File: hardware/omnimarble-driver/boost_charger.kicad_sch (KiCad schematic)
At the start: 42 parts, among them K1 HF3FF-12V, K2 HF3FF-12V, Q1 MMBT3904, Q2 MMBT3904, Q3 MMBT3904, Q91 AOD66923, U4 UC3843B, U5 CJ431

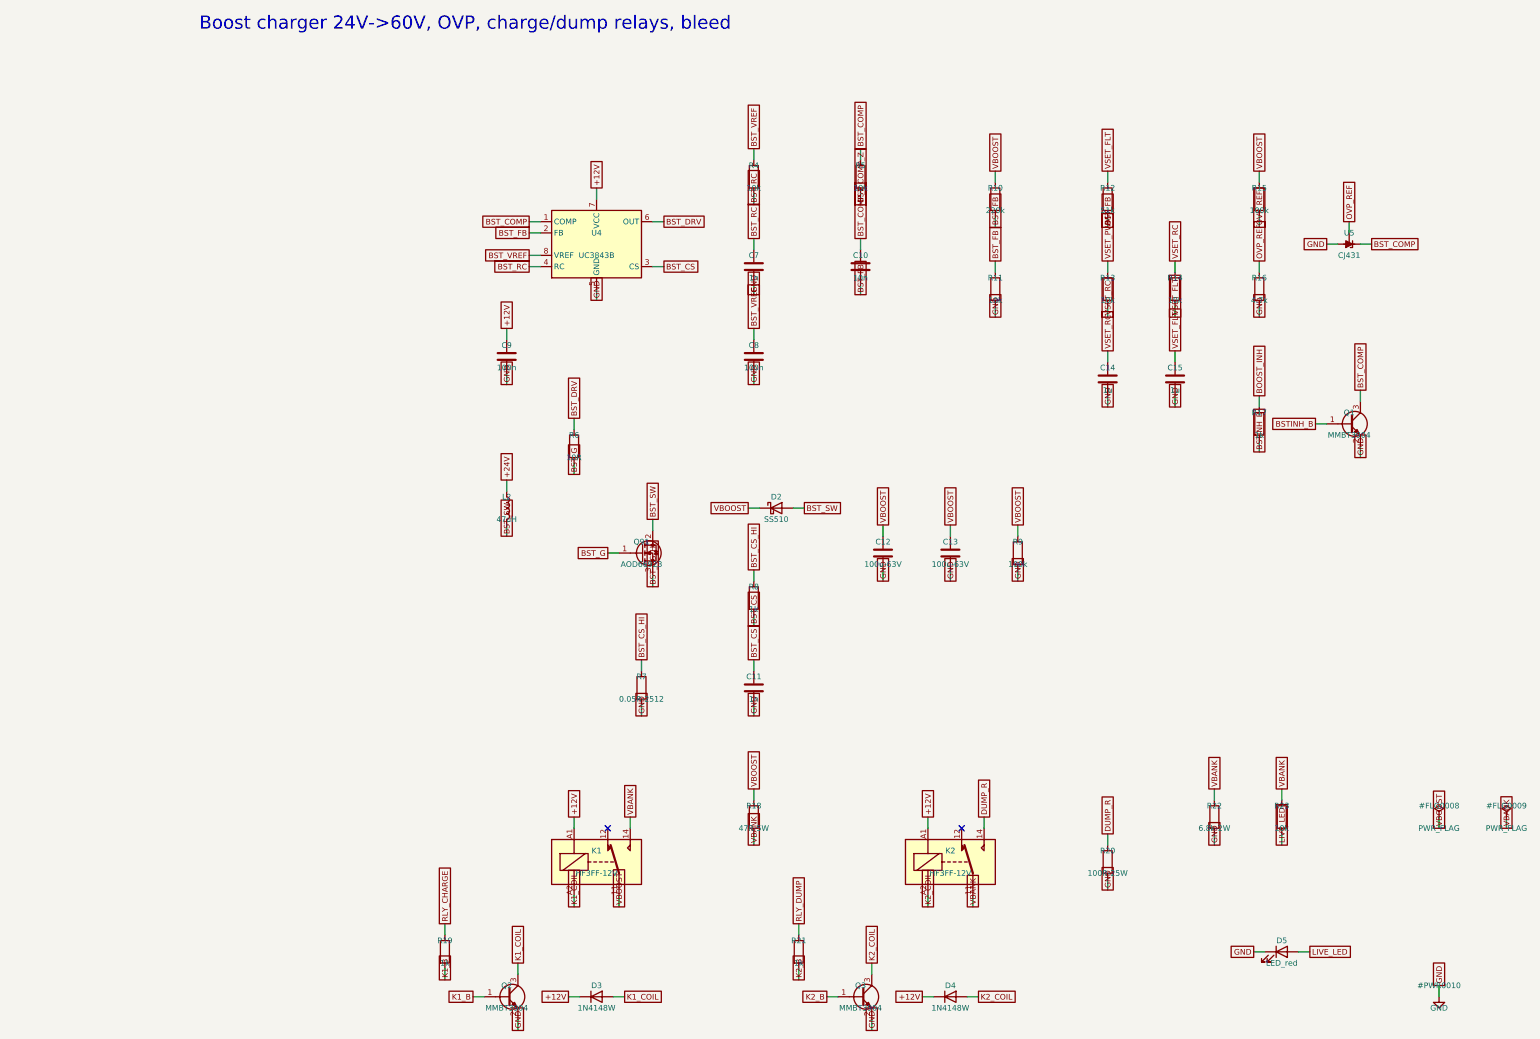
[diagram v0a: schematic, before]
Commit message: Address external design review: boost FB + OVP redesign, BOM freeze
Review findings accepted and fixed (each verified by machine check):

1. Boost feedback network was wrong (confirmed: as-drawn spanned
   54-68V with PWM inverted vs the comment). Redesigned: RT/RB/RJ =
   100k/10k/9.1k with the exact transfer function documented in the
   schematic and design-calcs.md. PWM=0 (MCU-dead state) commands
   55.0V; full PWM commands 18.7V (below the 24.5V converter floor).
   New calcs.py asserts both endpoints.
2. OVP tripped at 55.6V, not the claimed 63V (confirmed). Redesigned:
   CJ431 (+/-0.5%) + 100k/4.3k 1% -> 60.5V nominal, 59.1-62.0V across
   tolerances. Protection ladder asserted in calcs.py: 55V operating
   < 59.1V trip-min, 62.0V trip-max < 63V cap rating - 1V. Operating
   ceiling deliberately reduced 60->55V to keep the bands disjoint.
3. BOM/schematic controller split-brain: bom.csv was stale
   (pre-UC3843 swap); regenerated from parts.py. Both now UC3843B.
4. High-power placeholders now real orderable parts (LCSC-verified):
   47R/5W SQM cement C5807995, dump redesigned to 2x 100R/10W cement
   in series C216413 (no 20-25W part stocked on LCSC; 5.3s to <5V),
   50mR/3W 2512 C2994645, 63V/35V electrolytics C28241/C176666, 10uH
   Sunlord C79272, MINI fuses+Keystone 3568 holders, buzzer, Pico
   sockets/breakout headers. Single documented exception: the 6.8k/2W
   bleed (CRH2512J6K80E04Z) is marked ORDER-REVIEW because LCSC's
   search is uncrawlable - validate.py allowlists it visibly.
5. validate.py pulled forward from the fab phase: fails on unknown
   footprints, blank LCSC on machine-placed parts, missing Variant
   fields, and duplicate refs; generates per-variant gate-rail BOMs
   (bom_rail_emit/recv.csv). Caught two bad footprint names.
6. Paralleling constraints now on the schematic (same-lot FETs,
   symmetric copper, <25mm gate loops, driver return at shunt star).
7. Fail-safe defaults hardened: MCU_FIRE and FIRE_GATED get explicit
   pulldow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
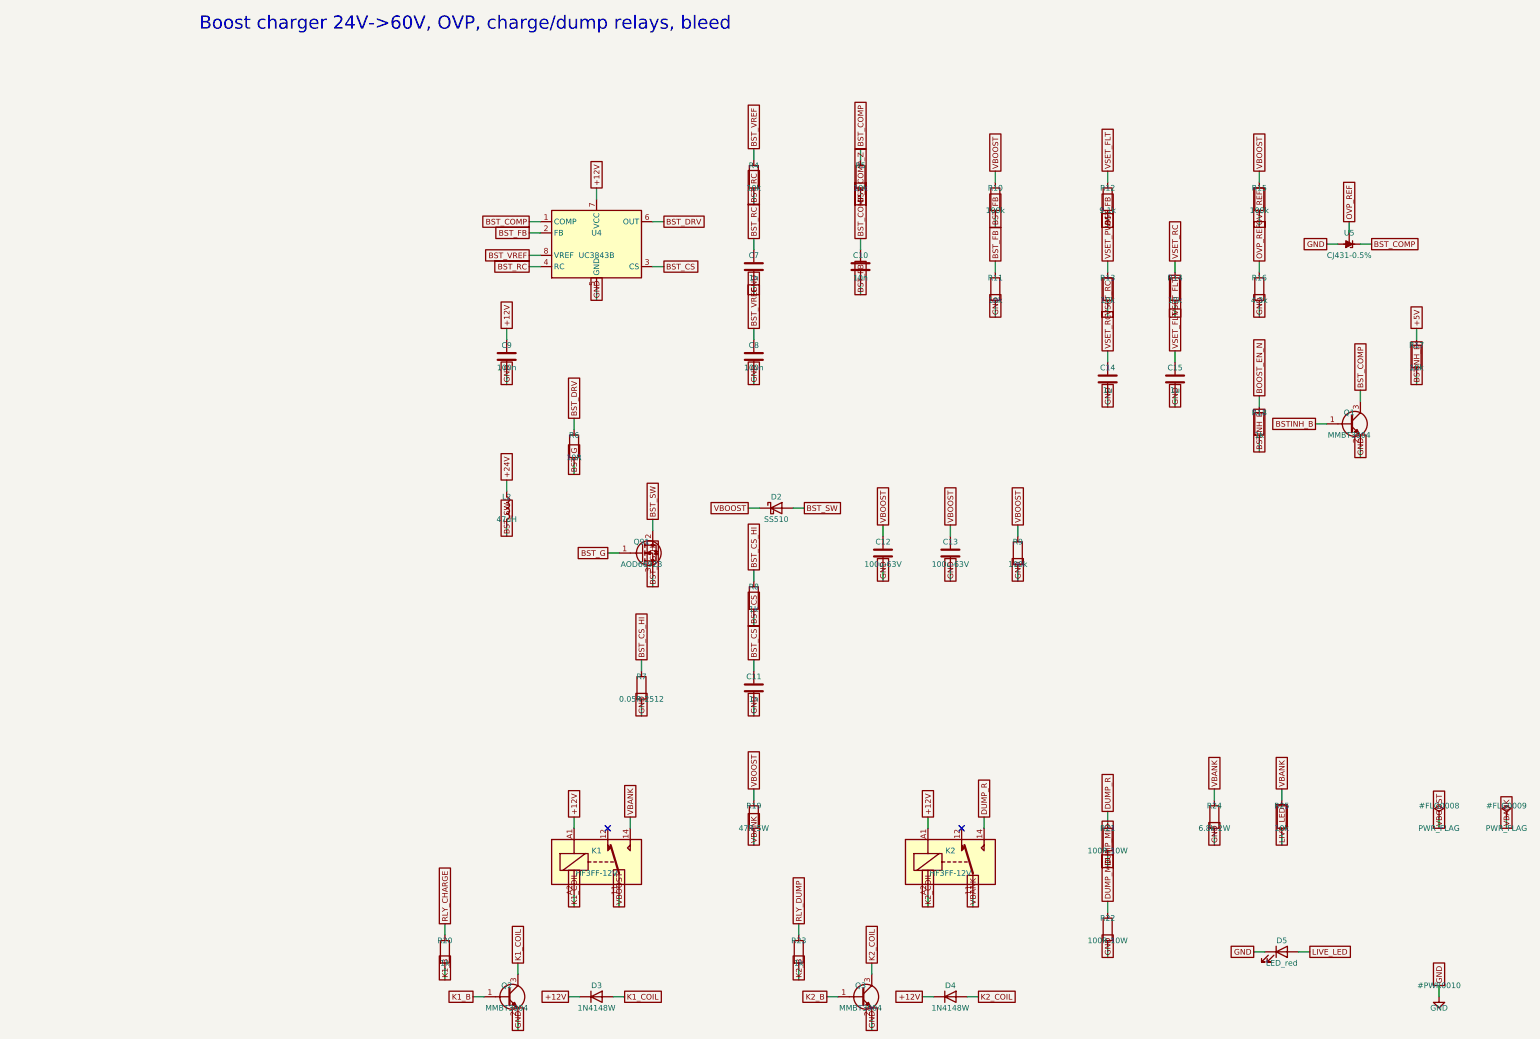
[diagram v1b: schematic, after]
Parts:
- added R24: 6.8k-2W, Resistor_SMD:R_2512_6332Metric, symbol Device:R
- added R25: 10k, Resistor_SMD:R_0603_1608Metric, symbol Device:R
- C10: LCSC (none) -> C57112
- C12, C13: LCSC (none) -> C28241
- R10: value 220k -> 100k; LCSC C22961 -> C25803
- R12: value 51k -> 9.1k; LCSC C23196 -> C23260
- R16: value 4.7k -> 4.3k; LCSC C23162 -> C23159
- R17: value 1k -> 10k; LCSC C21190 -> C25804
- R18: value 47R-5W -> 1k; footprint Resistor_SMD:R_2512_6332Metric -> Resistor_SMD:R_0603_1608Metric; LCSC (none) -> C21190
- R19: value 1k -> 47R-5W; footprint Resistor_SMD:R_0603_1608Metric -> Resistor_THT:R_Box_L26.0mm_W5.0mm_P20.00mm; LCSC C21190 -> C5807995
- R20: value 100R-25W -> 1k; footprint Resistor_SMD:R_2512_6332Metric -> Resistor_SMD:R_0603_1608Metric; LCSC (none) -> C21190
- R21: value 1k -> 100R-10W; footprint Resistor_SMD:R_0603_1608Metric -> Resistor_THT:R_Radial_Power_L11.0mm_W7.0mm_P5.00mm; LCSC C21190 -> C216413
- R22: value 6.8k-2W -> 100R-10W; footprint Resistor_SMD:R_2512_6332Metric -> Resistor_THT:R_Radial_Power_L11.0mm_W7.0mm_P5.00mm; LCSC (none) -> C216413
- R23: value 10k -> 1k; LCSC C25804 -> C21190
- R7: LCSC (none) -> C2994645
- U5: value CJ431 -> CJ431-0.5%
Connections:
- net BSTINH_B: now also R18.2
- net DUMP_R: now also R21.1; no longer R20.1
- net GND: now also R24.2; no longer R20.2
- net K1_B: now also R20.2; no longer R19.2
- net K2_B: now also R23.2; no longer R21.2
- net LIVE_LED: now also R25.2; no longer R23.2
- net RLY_CHARGE: now also R20.1; no longer R19.1
- net RLY_DUMP: now also R23.1; no longer R21.1
- net VBANK: now also R19.2, R24.1, R25.1; no longer R18.2, R22.1, R23.1
- net VBOOST: now also R19.1; no longer R18.1
- net BOOST_INH renamed +5V
- new net BOOST_EN_N: R18.1
- new net DUMP_MID: R21.2, R22.1

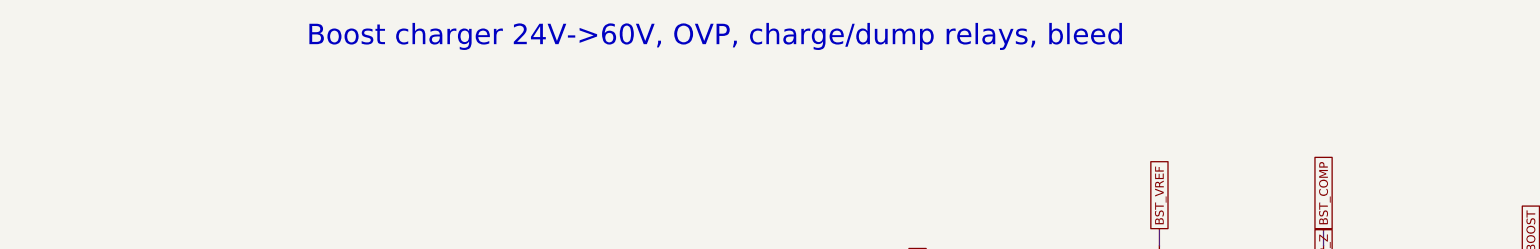
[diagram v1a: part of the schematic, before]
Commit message: Re-audit hygiene fixes: stale labels, COMMON variant, production gate
All six re-audit findings addressed:
1. Rail variant BOMs now include Variant=COMMON parts (J1 RAIL-IDC
   appears in both bom_rail_emit.csv and bom_rail_recv.csv).
2. design-calcs.md headings derive from V_BANK_MAX instead of
   hardcoded "60V" strings.
3. OVP reference wording unified to CJ431 +/-0.5% everywhere (the
   math already used ref_tol=0.005; text now matches).
4. Stale "57.2V OVP floor" magic number in the boost comment replaced
   with a reference to the calcs.py protection-ladder asserts.
5. validate.py --production mode: ORDER-REVIEW placeholder LCSC
   values fail (exit 1) at fab/assembly export; review mode warns.
   Verified: production exit code 1 on the 6.8k bleed placeholder.
6. Boost capability wording is now "24.5-55V operating (63V-rated
   bank)" in the schematic, sheet comments, and parts.py.

Re-verified: calcs 18/18 PASS, ERC 0 both projects, netlist
assertions pass, validate review-mode PASS with visible WARN,
rail BOMs 13/7 parts. PDFs refreshed.

Co-Authored-By: Claude Fable 5 <noreply@anthropic.com>
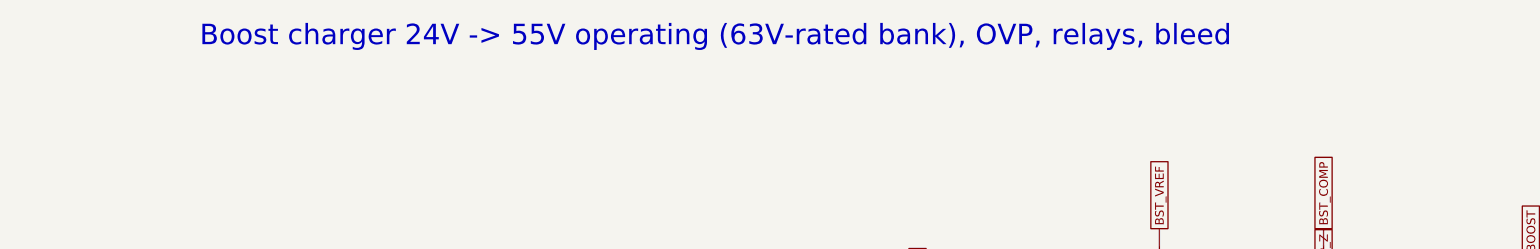
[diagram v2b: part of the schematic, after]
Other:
- note added: "Boost charger 24V -> 55V operating (63V-rated bank), OVP, relays, bleed"
- note removed: "Boost charger 24V->60V, OVP, charge/dump relays, bleed"

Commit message: Datasheet-exact footprints, placement engine, scripted PCB router WIP
- gen_footprints.py: TOLL-8, D2PAK (cathode-tab corrected), 5930 shunt,
  9.5mm barrier, HF3FF relay land patterns; drop _DRAFT footprints
- placement.py: 220x150 board plan, pulse zone polygons derived from
  package pad windows, shelf-packed clusters, Kelvin/manual tracks
- gen_pcb.py: netlist->board generator with zone builder, via stitching,
  pad-in-zone assertions, straggler/GND-drop/escape pre-routes and a
  negotiated-congestion (PathFinder-lite) signal router + greedy cleanup
- debug_route.py/debug_map.py/debug_j7.py: router diagnostics

Co-Authored-By: Claude Fable 5 <noreply@anthropic.com>
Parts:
- K1, K2: footprint omnimarble:Relay_HF3FF_T73_DRAFT -> omnimarble:Relay_HF3FF_T73

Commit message: Driver PCB: resolve review blockers (2oz trace width, R24 BOM, validators)
External review caught real fab-readiness issues; all resolved:
- BLOCKER 2oz trace width: ISNS Kelvin pair was 0.1mm (a 1oz spec; JLC 2oz min
  trace/space is 0.15mm). Widened to 0.15mm -> ~0.17mm pair spacing (both >=
  0.15mm 2oz min). Scoped `isns_kelvin_pair` rule in .kicad_dru blesses the
  sub-0.2mm pair spacing (A.NetName match); clearance to all other nets stays
  0.2mm. min_track_width -> 0.15.
- MAJOR width source-of-truth: NET_WIDTHS["ISNS_P/N"]=0.15 is now the single
  value; local_finish narrows to it, validate_widths checks it -> PASS.
- BLOCKER R24 6.8k-2W BOM placeholder: no verified JLC C-number and 2W is
  marginal in 2512 -> marked LCSC=HAND-INSTALL (explicit, exclude from CPL,
  user-sourced). validate.py --production PASSes with a NOTE.
- MAJOR check_netlist GATE1-6: stale J11 assertion (breakout removed) ->
  asserts comparator + Pico-socket topology. All netlist assertions PASS.
- CONCERN gate-drive route inequality: documented as an explicit WAIVER in
  BOARD_OVERVIEW.md (per-FET gate resistors + us-scale pulse app mitigate).
- Fixed the wrong 0.089mm/1oz capability claim in BOARD_OVERVIEW + memory.

Final: 0 electrical DRC / 0 unconnected / 0 parity; validate + validate_widths
+ check_netlist + calcs all PASS; 14 cosmetic silk warnings.

Co-Authored-By: Claude Fable 5 <noreply@anthropic.com>
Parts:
- R24: LCSC ORDER-REVIEW -> HAND-INSTALL
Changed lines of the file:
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@@
 			)
 		)
-		(property "LCSC" "ORDER-REVIEW"
+		(property "LCSC" "HAND-INSTALL"
 			(at 199.39 199.39 0)
 			(show_name no)

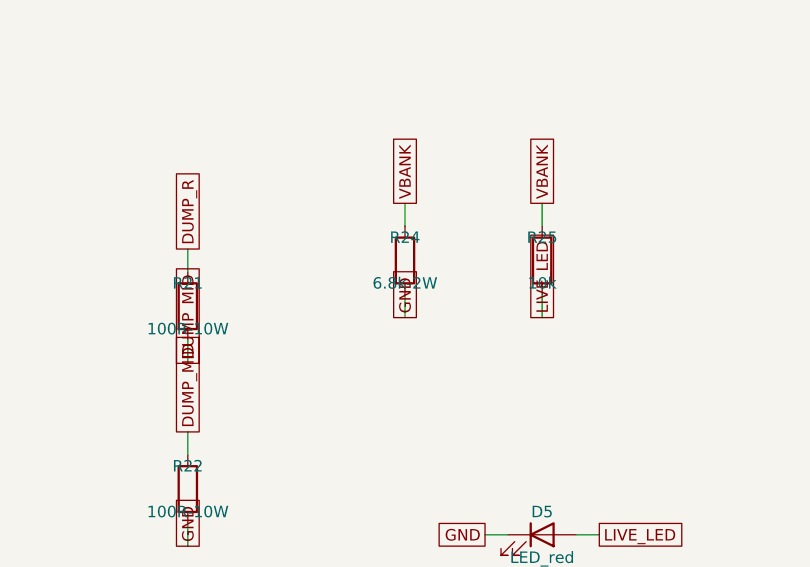
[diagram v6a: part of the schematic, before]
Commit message: Driver PCB: resolve R24 to a real JLC-placed part (6.8k 1W 2512, C26073)
The "6.8k 2W" spec was inconsistent -- a 2512 is a ~1W package, and LCSC stock
confirms it: every 6.8k 2512 that's in stock is 1W; the 1.5W and 2W variants
are all 0-stock. Actual dissipation is 55^2/6800 = 0.44W, so 1W carries it with
2.2x margin. R24 -> value "6.8k", LCSC C26073 (UNI-ROYAL 25121WJ0682T4E, 6.8k
2512 1W 5%, stock 3660) -- same UNI-ROYAL family as the board's other Rs.

No longer hand-install: validate.py --production PASSES with R24 as a placed
part (no NOTE). Every part on the board is now JLC-placeable. BOARD_OVERVIEW
updated. All validators + DRC still green.

Co-Authored-By: Claude Fable 5 <noreply@anthropic.com>
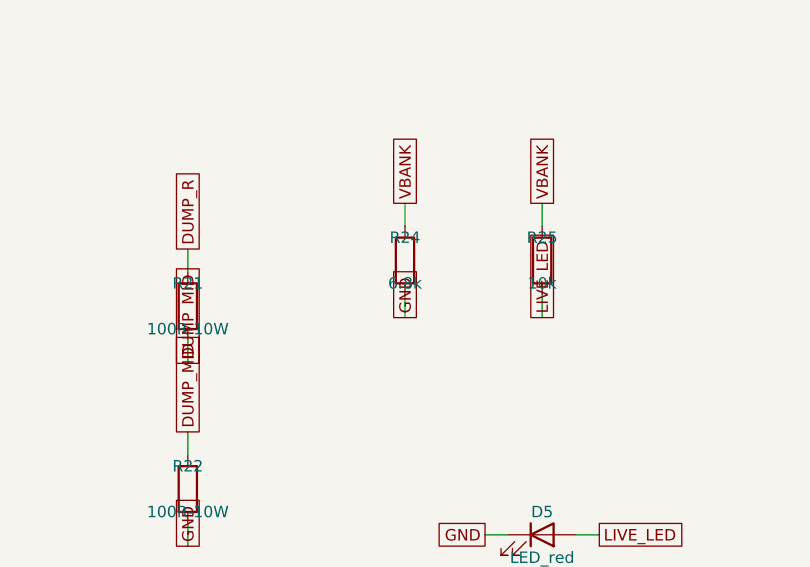
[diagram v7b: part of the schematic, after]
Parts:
- R24: value 6.8k-2W -> 6.8k; LCSC HAND-INSTALL -> C26073
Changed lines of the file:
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@@
 			)
 		)
-		(property "Value" "6.8k-2W"
+		(property "Value" "6.8k"
 			(at 199.39 201.93 0)
 			(show_name no)
@@
 			)
 		)
-		(property "LCSC" "HAND-INSTALL"
+		(property "LCSC" "C26073"
 			(at 199.39 199.39 0)
 			(show_name no)
